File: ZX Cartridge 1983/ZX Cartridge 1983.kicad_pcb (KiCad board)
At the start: 2 copper layers, 57.9 x 61.6 mm, 19 parts, among them J1 Cartridge, M1 Mounting, M2 Mounting, M3 Mounting, M4 Mounting, SW1 ROM_SEL, U1 27C020, U2 MC14495P1

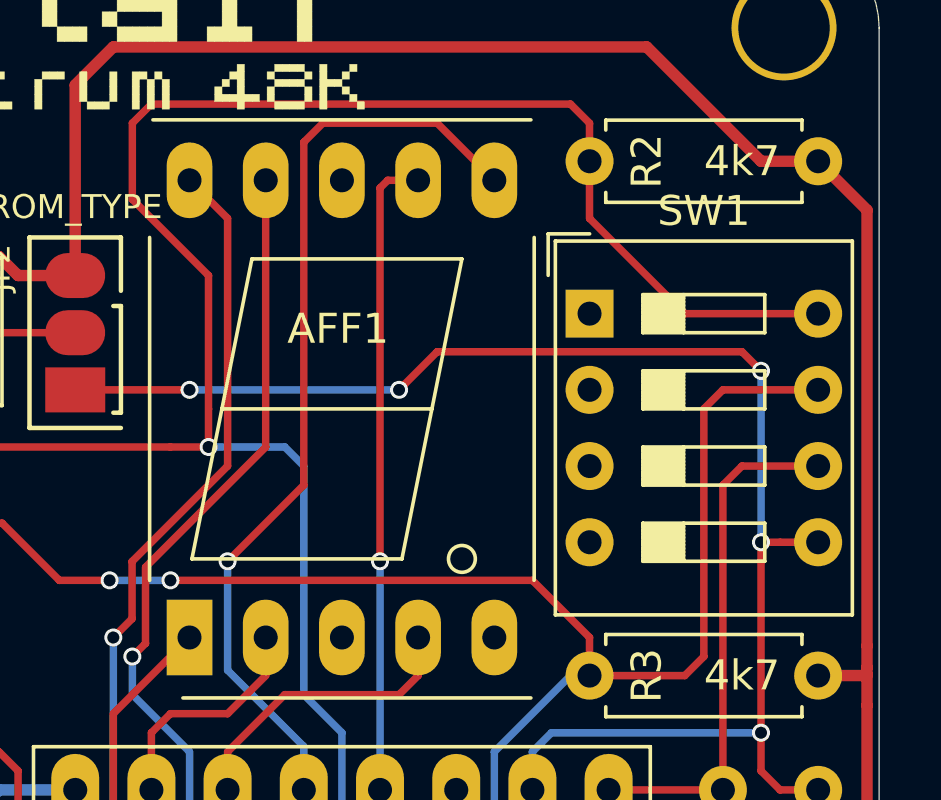
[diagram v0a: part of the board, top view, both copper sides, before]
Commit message: Silkscreen tweaks
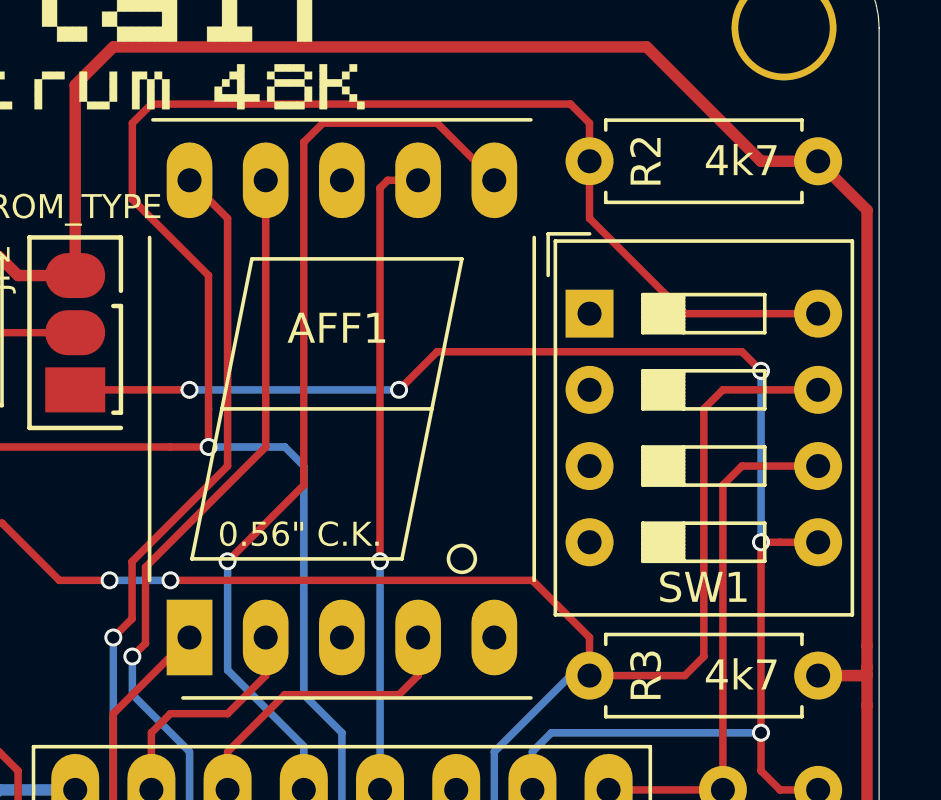
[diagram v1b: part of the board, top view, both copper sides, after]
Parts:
- AFF1: value LTS-6980HR -> 0.56" C.K.

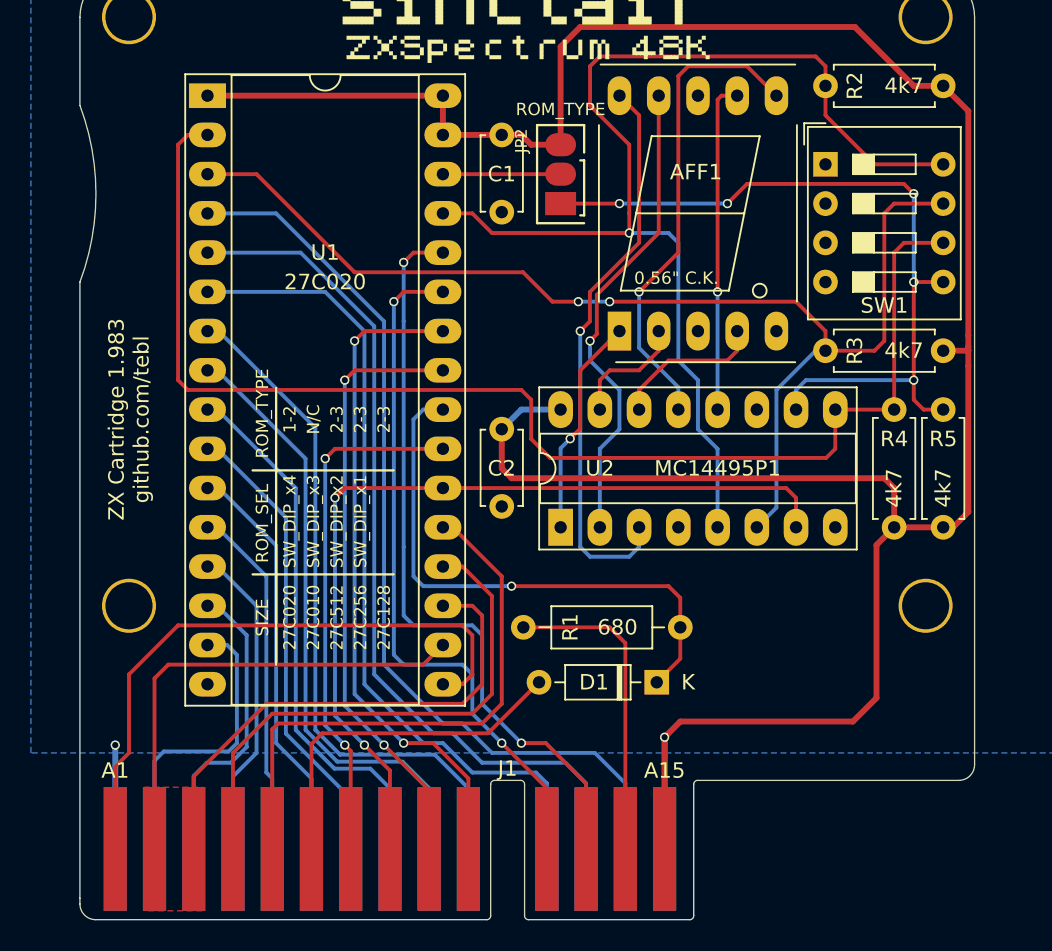
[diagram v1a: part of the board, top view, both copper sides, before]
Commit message: Moved pins to line up with original Kempson Pro Joystick interface
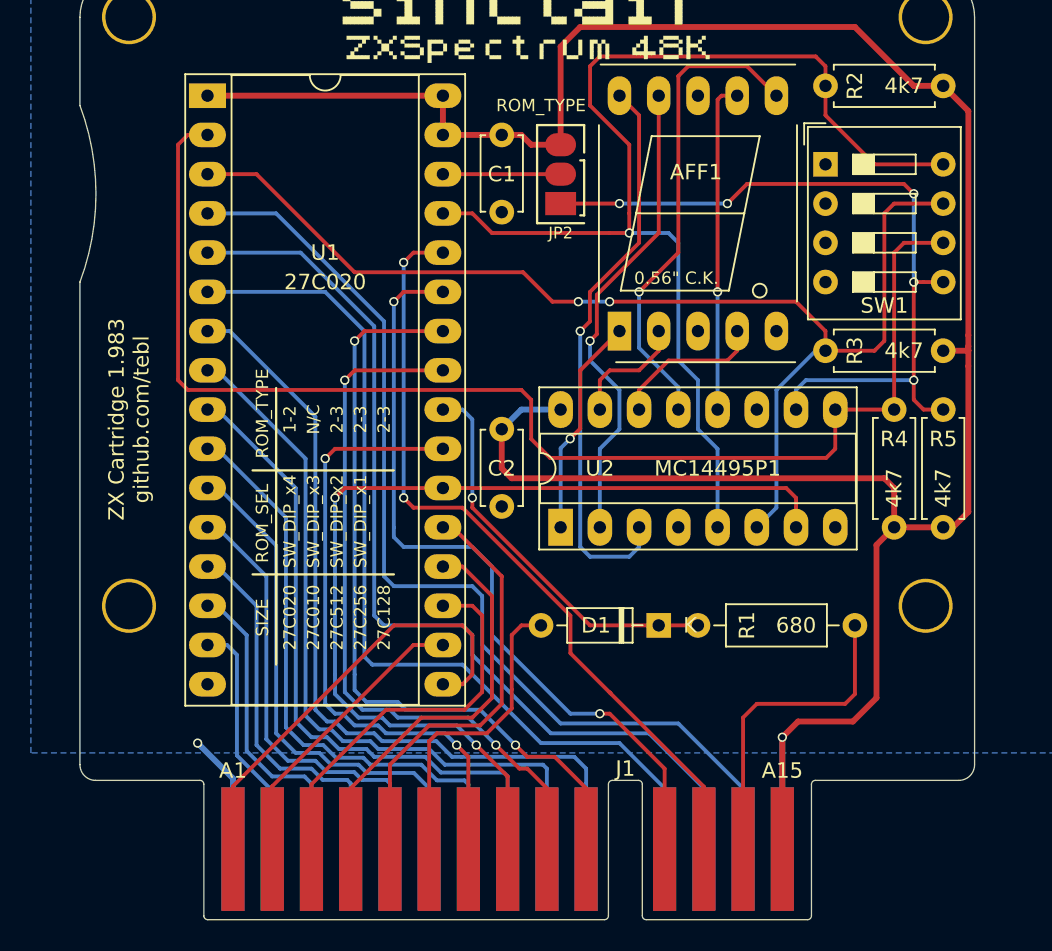
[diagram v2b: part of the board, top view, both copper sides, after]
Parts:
- moved R1 21.5 mm to (170.4, 101.6), turned to 180 degrees
- moved J1 7.62 mm to (158.1, 116.1)
- moved D1 3.69 mm to (157.7, 101.6)
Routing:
- net /D4: track 30.6 -> 18.9 mm
- net /D3: track 40.2 -> 28.8 mm
- net /~ROM_OE: track 36.3 -> 25.6 mm
- net /D7: track 36.7 -> 27.7 mm
- net /D6: track 34.9 -> 26.1 mm
- net /A5: track 44.5 -> 52.6 mm
- net /A2: track 30.1 -> 38.0 mm
- net /A4: track 39.8 -> 47.6 mm
- net /A3: track 35.1 -> 42.8 mm
- net VCC: track 169.5 -> 161.8 mm
- net /D5: track 33.1 -> 25.5 mm
- net /A11: track 39.2 -> 46.4 mm
- net /A9: track 43.0 -> 50.1 mm
- net /A1: track 26.6 -> 33.5 mm
- net /A10: track 33.8 -> 40.4 mm
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- removed copper zone on F.Cu, net VCC
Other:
- outline, holes or cut-outs redrawn

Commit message: Marked pinouts for smaller chips
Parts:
- U1: footprint Package_DIP:DIP-32_W15.24mm_Socket_LongPads -> 27c020:DIP-32_W15.24mm_Socket_LongPads

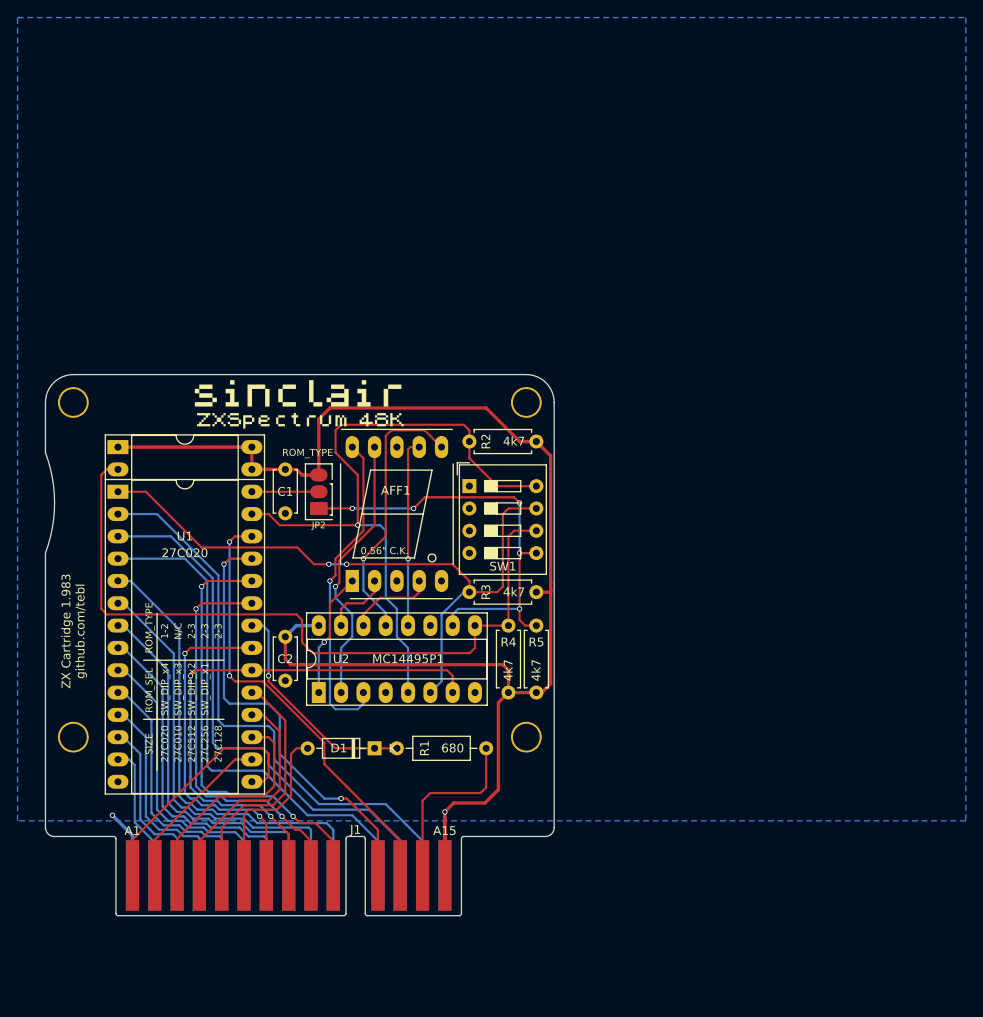
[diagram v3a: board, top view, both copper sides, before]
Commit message: Cartridge 1.983 needed some more height to clear RAM turbo interface case
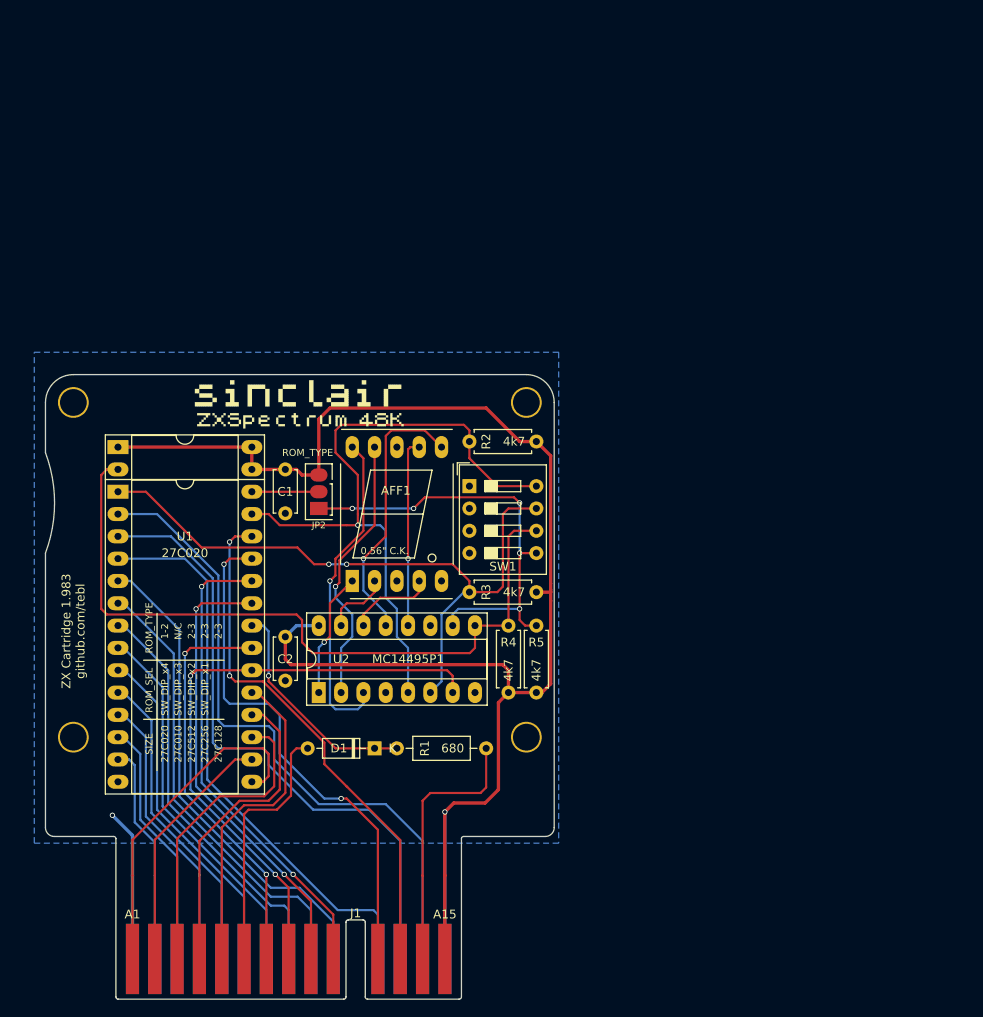
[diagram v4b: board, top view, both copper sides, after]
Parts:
- moved J1 9.50 mm to (158.1, 125.6)
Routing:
- net VCC: track 161.8 -> 180.8 mm
- net /D6: track 26.1 -> 35.6 mm
- net /D2: track 15.7 -> 25.2 mm
- net GND: track 7.80 -> 17.3 mm
- net /D7: track 27.7 -> 37.2 mm
- net /D5: track 25.5 -> 35.0 mm
- net /D4: track 18.9 -> 28.4 mm
- net /D3: track 28.8 -> 38.3 mm
- net /A8: track 50.2 -> 59.7 mm
- net /A15: track 20.8 -> 30.3 mm
- net /A14: track 20.1 -> 29.6 mm
- net /A13: track 50.8 -> 60.3 mm
- net /A12: track 65.6 -> 75.1 mm
- net /A7: track 62.1 -> 71.6 mm
- net /D1: track 20.1 -> 28.4 mm
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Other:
- board size 57.9 x 61.6 mm -> 57.9 x 71.1 mm
